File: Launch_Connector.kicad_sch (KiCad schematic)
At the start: 28 parts, among them J1 ADC1, J2 ADC2, J3 PWM, J4 GPIO

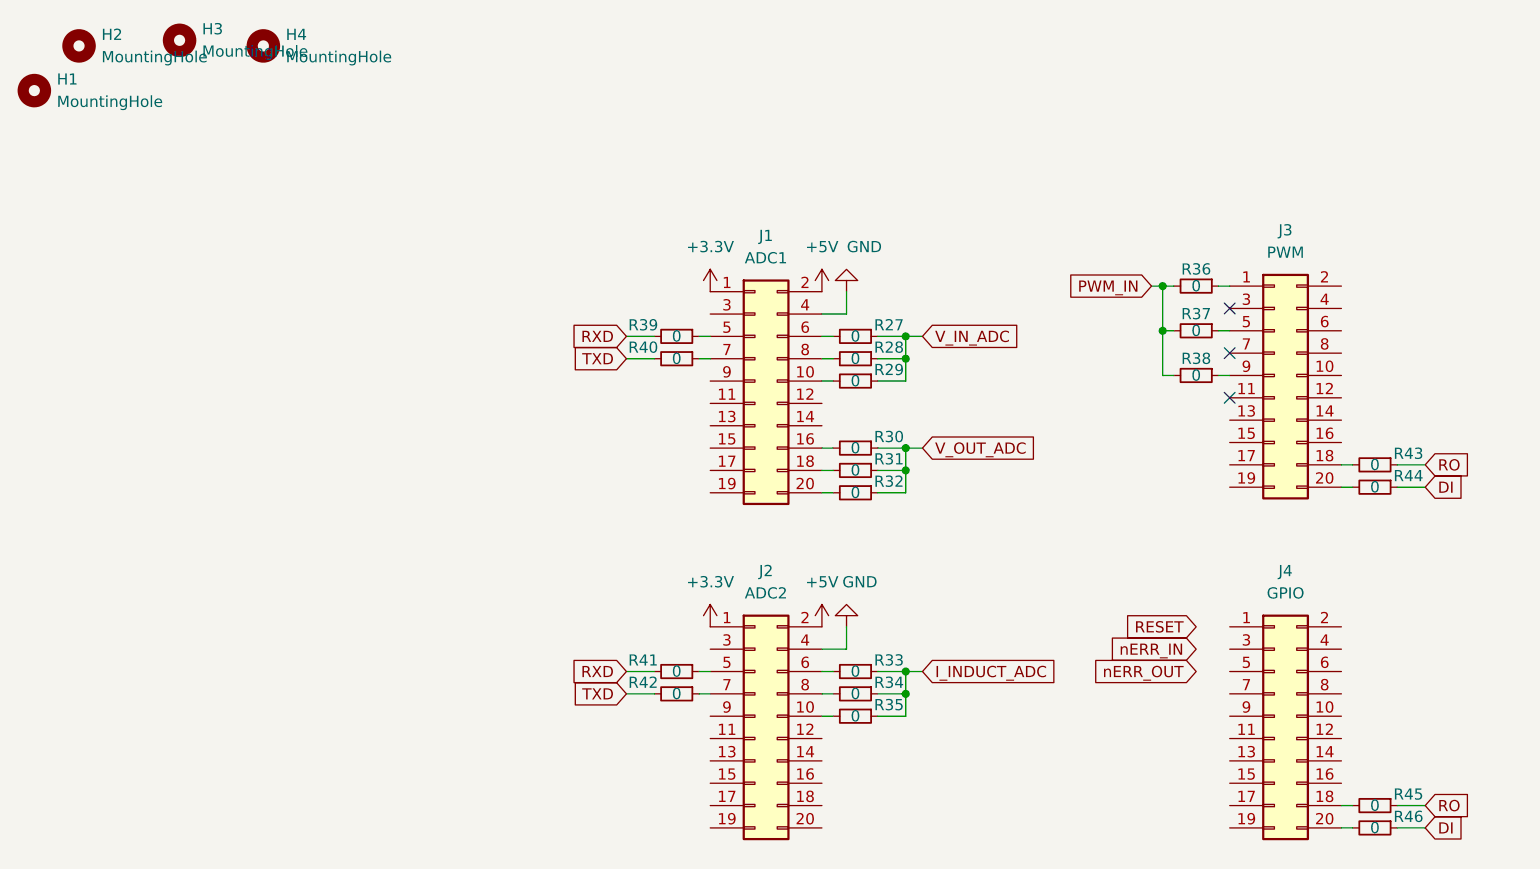
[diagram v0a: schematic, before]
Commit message: Добавил молексы и убрал питание
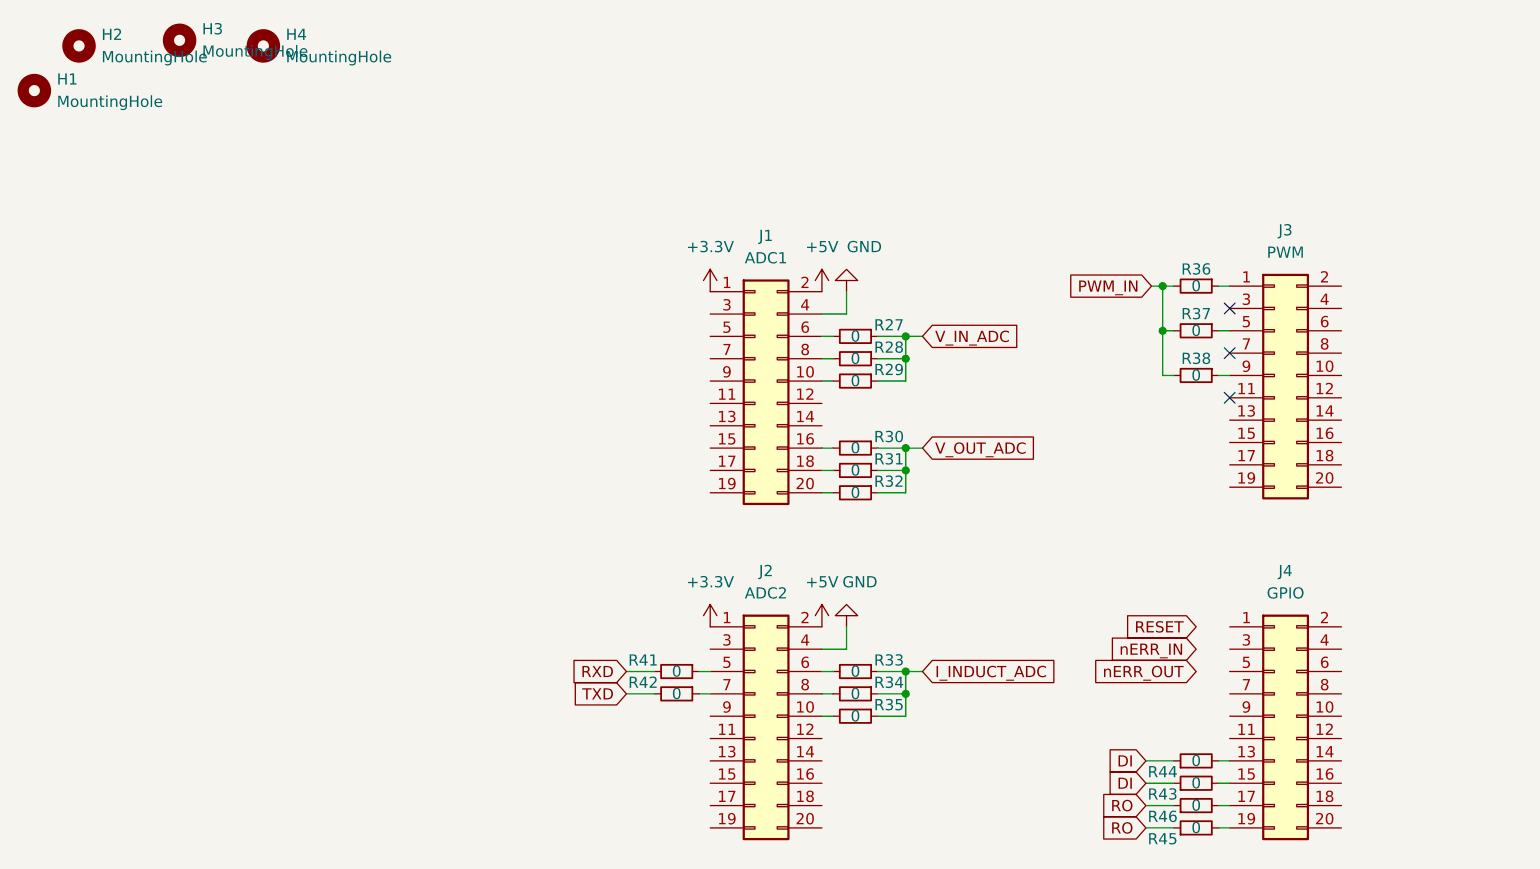
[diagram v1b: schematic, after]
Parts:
- removed R39, R40: 0, Resistor_SMD:R_0805_2012Metric_Pad1.20x1.40mm_HandSolder, symbol Device:R_Small
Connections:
- net DI: now also R43.1; no longer R46.1
- net RO: now also R46.1; no longer R43.1
- net at R45.2: now also J4.19 (Pin_19); no longer J4.18 (Pin_18)
- net at J4.13 (Pin_13): now also R44.2
- net at J4.15 (Pin_15): now also R43.2
- net at J4.17 (Pin_17): now also R46.2
- net at J4.20 (Pin_20): no longer R46.2
- net at J3.18 (Pin_18): no longer R43.2
- net at J3.20 (Pin_20): no longer R44.2
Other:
- moved on the sheet: R43, R44, R45, R46

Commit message: Первая версия в производство
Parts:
- removed R41, R42: 0, Resistor_SMD:R_0805_2012Metric_Pad1.20x1.40mm_HandSolder, symbol Device:R_Small
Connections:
- net RXD: now also J1.7 (Pin_7)
- net TXD: now also J1.5 (Pin_5)
- net at R45.2: now also J4.15 (Pin_15); no longer J4.19 (Pin_19)
- net at J4.11 (Pin_11): now also R43.2
- net at J4.13 (Pin_13): now also R46.2; no longer R44.2
- net at J4.17 (Pin_17): no longer R46.2
- net at J4.9 (Pin_9): now also R44.2
- net RESET_GPIO: now reaches J3.13 (Pin_13)
- net nERR_IN_GPIO: now reaches J3.15 (Pin_15)
- net Relay_Control: now reaches J3.18 (Pin_18)
- no-connect marks 3 -> 53
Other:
- moved on the sheet: J1, J3, R27, R28, R29, R30, R31, R32, R36, R37, R38, R43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

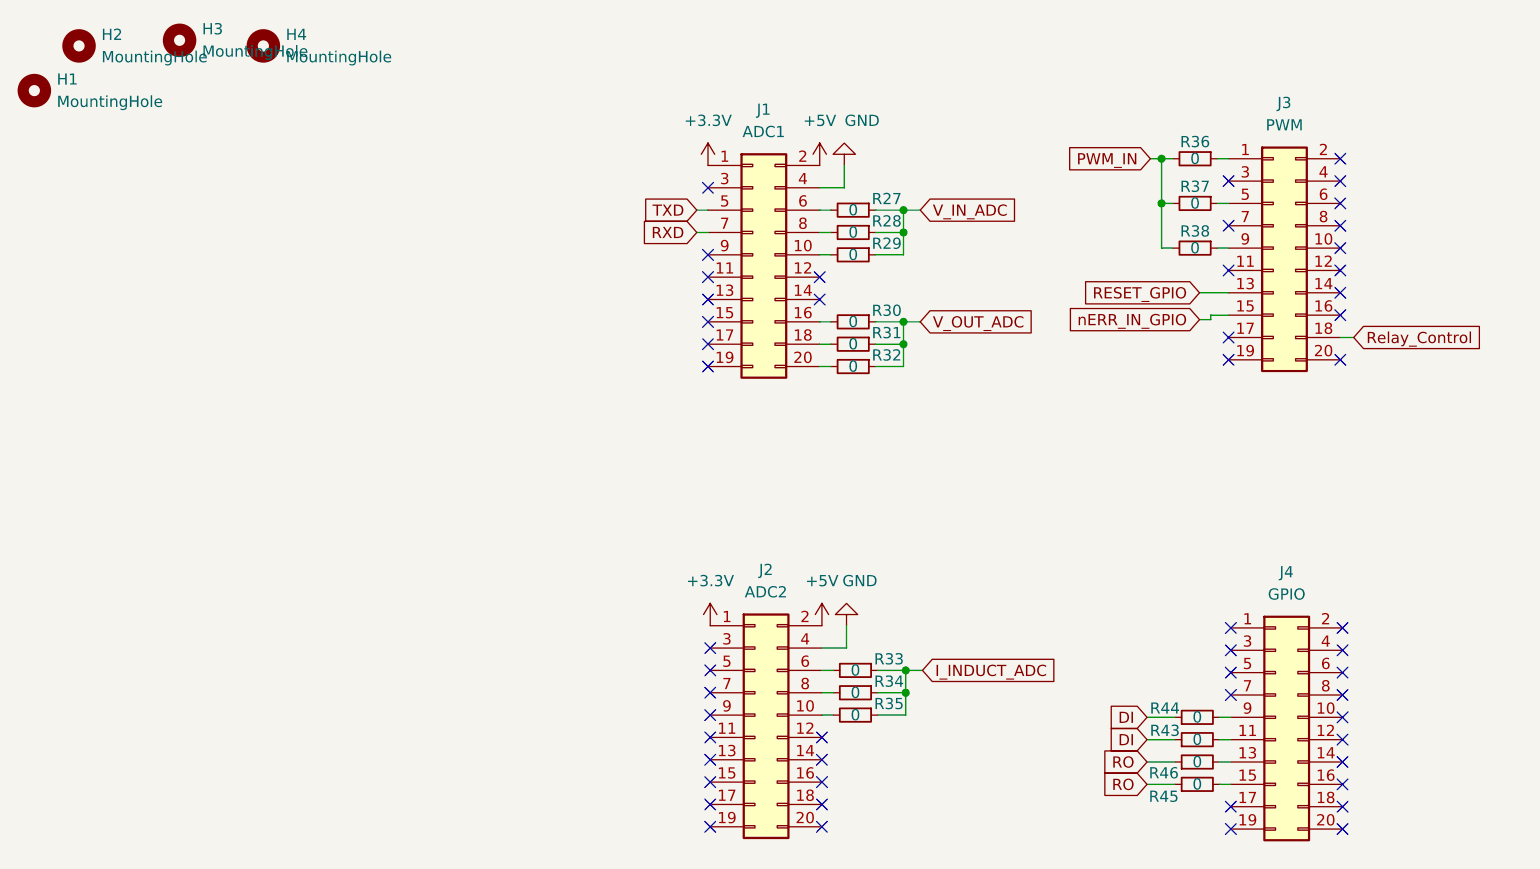
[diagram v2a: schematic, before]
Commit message: Добавил температуру, убрал подтяжки RS-485, заменил ШИМ на дифференциальный сигнал, добавил земли RS-485
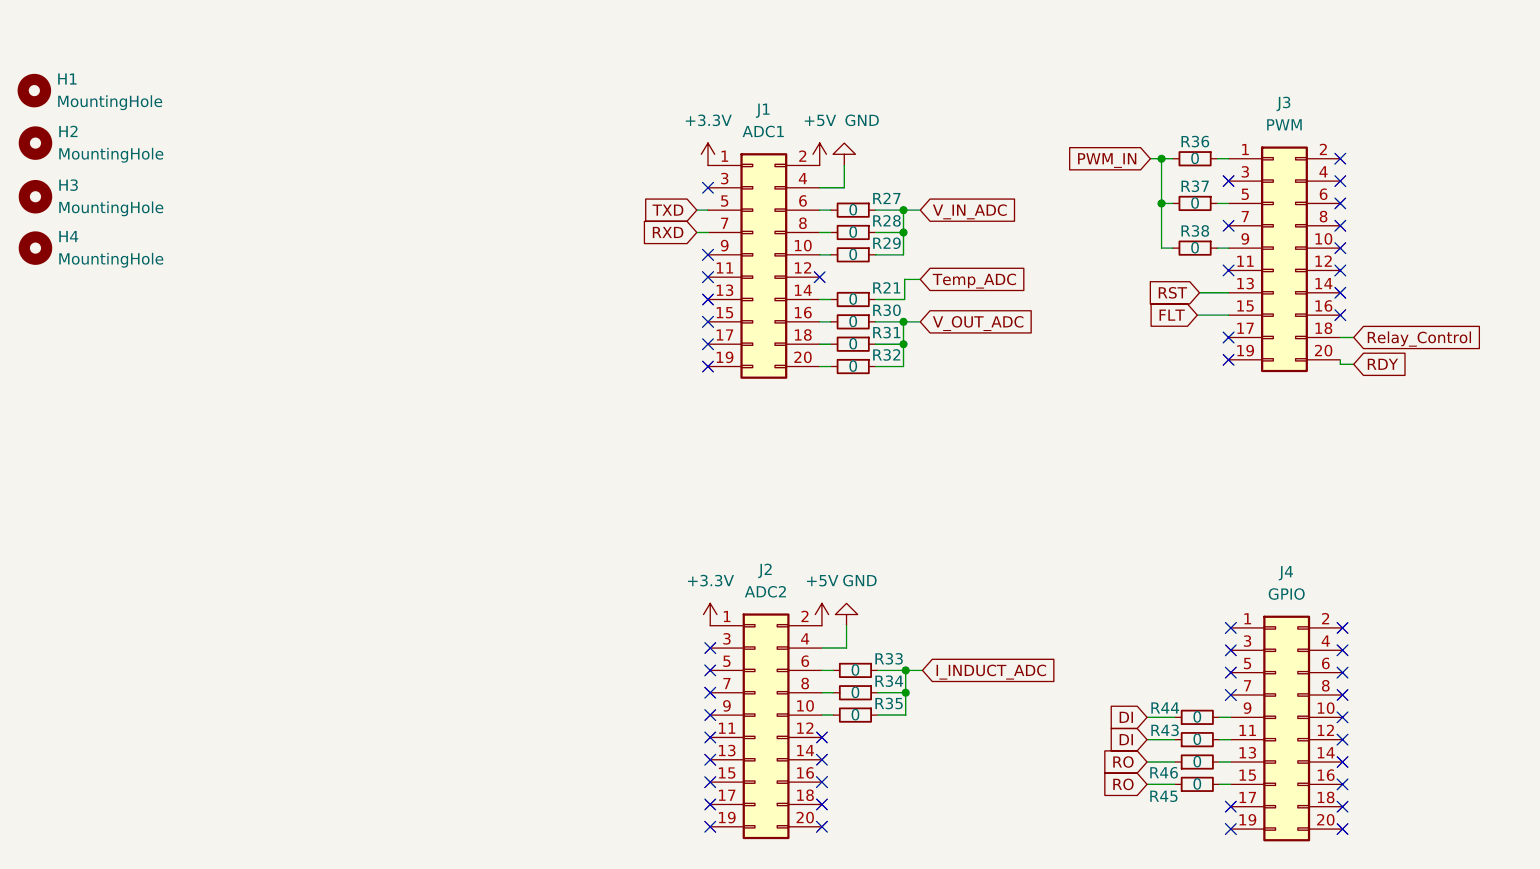
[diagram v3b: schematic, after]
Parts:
- added R21: 0, Resistor_SMD:R_0805_2012Metric_Pad1.20x1.40mm_HandSolder, symbol Device:R_Small
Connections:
- net at J1.14 (Pin_14): now also R21.2
- net RDY: now reaches J3.20 (Pin_20)
- net RESET_GPIO renamed RST
- net nERR_IN_GPIO renamed FLT
- new net Temp_ADC: R21.1
- no-connect marks 53 -> 51
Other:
- moved on the sheet: H2, H3, H4
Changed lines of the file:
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@@
   (no_connect (at 177.038 64.262))
   (no_connect (at 177.038 66.802))
-  (no_connect (at 177.038 74.422))
   (no_connect (at 177.038 69.342))
   (no_connect (at 177.038 54.102))
@@
   (no_connect (at 105.156 62.484))
   (no_connect (at 164.338 71.882))
-  (no_connect (at 117.856 67.564))
   (no_connect (at 117.856 65.024))
   (no_connect (at 164.338 54.102))
@@
     (stroke (width 0) (type default) (color 0 0 0 0))
   )
+  (wire (pts (xy 178.562 74.93) (xy 177.038 74.93))
+    (stroke (width 0) (type default) (color 0 0 0 0))
+  )
   (wire (pts (xy 118.11 107.188) (xy 120.904 107.188))
     (stroke (width 0) (type default) (color 0 0 0 0))
@@
     (stroke (width 0) (type default) (color 0 0 0 0))
   )
+  (wire (pts (xy 177.038 74.93) (xy 177.038 74.422))
+    (stroke (width 0) (type default) (color 0 0 0 0))
+  )
   (wire (pts (xy 120.65 54.864) (xy 120.65 52.324))
     (stroke (width 0) (type default) (color 0 0 0 0))
@@
     (stroke (width 0) (type default) (color 0 0 0 0))
   )
-  (wire (pts (xy 162.306 69.85) (xy 162.306 69.342))
-    (stroke (width 0) (type default) (color 0 0 0 0))
-  )
-  (wire (pts (xy 164.338 69.342) (xy 162.306 69.342))
+  (wire (pts (xy 160.782 69.342) (xy 164.338 69.342))
     (stroke (width 0) (type default) (color 0 0 0 0))
   )
@@
     (stroke (width 0) (type default) (color 0 0 0 0))
   )
-  (wire (pts (xy 161.036 69.85) (xy 162.306 69.85))
-    (stroke (width 0) (type default) (color 0 0 0 0))
-  )
   (wire (pts (xy 118.11 112.268) (xy 119.38 112.268))
     (stroke (width 0) (type default) (color 0 0 0 0))
@@
     (stroke (width 0) (type default) (color 0 0 0 0))
   )
+  (wire (pts (xy 117.856 67.564) (xy 119.126 67.564))
+    (stroke (width 0) (type default) (color 0 0 0 0))
+  )
   (wire (pts (xy 156.718 56.642) (xy 157.988 56.642))
     (stroke (width 0) (type default) (color 0 0 0 0))
@@
     (stroke (width 0) (type default) (color 0 0 0 0))
   )
+  (wire (pts (xy 127.508 65.278) (xy 127.508 67.564))
+    (stroke (width 0) (type default) (color 0 0 0 0))
+  )
   (wire (pts (xy 117.856 70.104) (xy 119.126 70.104))
     (stroke (width 0) (type default) (color 0 0 0 0))
@@
     (stroke (width 0) (type default) (color 0 0 0 0))
   )
+  (wire (pts (xy 129.286 65.278) (xy 127.508 65.278))
+    (stroke (width 0) (type default) (color 0 0 0 0))
+  )
   (wire (pts (xy 158.242 117.602) (xy 155.067 117.602))
     (stroke (width 0) (type default) (color 0 0 0 0))
@@
     (stroke (width 0) (type default) (color 0 0 0 0))
   )
+  (wire (pts (xy 127.508 67.564) (xy 124.206 67.564))
+    (stroke (width 0) (type default) (color 0 0 0 0))
+  )
   (wire (pts (xy 163.068 61.722) (xy 164.338 61.722))
     (stroke (width 0) (type default) (color 0 0 0 0))
@@
     )
   )
-  (global_label "RESET_GPIO" (shape input) (at 161.036 66.802 180) (fields_autoplaced)
-    (effects (font (size 1.27 1.27)) (justify right))
-    (property "Intersheet References" "${INTERSHEET_REFS}" (id 0) (at 147.4348 66.7226 0)
-      (effects (font (size 1.27 1.27)) (justify right) hide)
+  (global_label "RST" (shape input) (at 161.036 66.802 180) (fields_autoplaced)
+    (effects (font (size 1.27 1.27)) (justify right))
+    (property "Intersheet References" "${INTERSHEET_REFS}" (id 0) (at 155.1758 66.7226 0)
+      (effects (font (size 1.27 1.27)) (justify right) hide)
+    )
+  )
+  (global_label "RDY" (shape input) (at 178.562 74.93 0) (fields_autoplaced)
+    (effects (font (size 1.27 1.27)) (justify left))
+    (property "Intersheet References" "${INTERSHEET_REFS}" (id 0) (at 184.6037 74.8506 0)
+      (effects (font (size 1.27 1.27)) (justify left) hide)
     )
   )
@@
     )
   )
+  (global_label "Temp_ADC" (shape input) (at 129.286 65.278 0) (fields_autoplaced)
+    (effects (font (size 1.27 1.27)) (justify left))
+    (property "Intersheet References" "${INTERSHEET_REFS}" (id 0) (at 141.1939 65.1986 0)
+      (effects (font (size 1.27 1.27)) (justify left) hide)
+    )
+  )
   (global_label "PWM_IN" (shape input) (at 155.448 51.562 180) (fields_autoplaced)
     (effects (font (size 1.27 1.27)) (justify right))
@@
     )
   )
-  (global_label "nERR_IN_GPIO" (shape input) (at 161.036 69.85 180) (fields_autoplaced)
-    (effects (font (size 1.27 1.27)) (justify right))
-    (property "Intersheet References" "${INTERSHEET_REFS}" (id 0) (at 145.4391 69.7706 0)
+  (global_label "FLT" (shape input) (at 160.782 69.342 180) (fields_autoplaced)
+    (effects (font (size 1.27 1.27)) (justify right))
+    (property "Intersheet References" "${INTERSHEET_REFS}" (id 0) (at 155.2846 69.2626 0)
       (effects (font (size 1.27 1.27)) (justify right) hide)
     )
@@
     (pin "2")
   )
-  (symbol (lib_id "Mechanical:MountingHole") (at 45.085 38.1 0) (unit 1)
-    (in_bom yes) (on_board yes) (fields_autoplaced)
-    (property "Reference" "H3" (id 0) (at 47.625 36.8299 0)
+  (symbol (lib_id "Mechanical:MountingHole") (at 28.702 55.88 0) (unit 1)
+    (in_bom yes) (on_board yes) (fields_autoplaced)
+    (property "Reference" "H3" (id 0) (at 31.242 54.6099 0)
       (effects (font (size 1.27 1.27)) (justify left))
     )
-    (property "Value" "MountingHole" (id 1) (at 47.625 39.3699 0)
+    (property "Value" "MountingHole" (id 1) (at 31.242 57.1499 0)
       (effects (font (size 1.27 1.27)) (justify left))
     )
-    (property "Footprint" "MountingHole:MountingHole_3.2mm_M3" (id 2) (at 45.085 38.1 0)
-      (effects (font (size 1.27 1.27)) hide)
-    )
-    (property "Datasheet" "~" (id 3) (at 45.085 38.1 0)
+    (property "Footprint" "MountingHole:MountingHole_3.2mm_M3" (id 2) (at 28.702 55.88 0)
+      (effects (font (size 1.27 1.27)) hide)
+    )
+    (property "Datasheet" "~" (id 3) (at 28.702 55.88 0)
       (effects (font (size 1.27 1.27)) hide)
     )
@@
     (pin "9")
   )
+  (symbol (lib_id "Device:R_Small") (at 121.666 67.564 270) (unit 1)
+    (in_bom yes) (on_board yes)
+    (property "Reference" "R21" (id 0) (at 125.476 66.294 90))
+    (property "Value" "0" (id 1) (at 121.666 67.564 90))
+    (property "Footprint" "Resistor_SMD:R_0805_2012Metric_Pad1.20x1.40mm_HandSolder" (id 2) (at 121.666 67.564 0)
+      (effects (font (size 1.27 1.27)) hide)
+    )
+    (property "Datasheet" "~" (id 3) (at 121.666 67.564 0)
+      (effects (font (size 1.27 1.27)) hide)
+    )
+    (pin "1")
+    (pin "2")
+  )
   (symbol (lib_id "Device:R_Small") (at 160.528 56.642 270) (unit 1)
     (in_bom yes) (on_board yes)
@@
     (pin "1")
   )
-  (symbol (lib_id "Mechanical:MountingHole") (at 33.655 38.735 0) (unit 1)
-    (in_bom yes) (on_board yes) (fields_autoplaced)
-    (property "Reference" "H2" (id 0) (at 36.195 37.4649 0)
+  (symbol (lib_id "Mechanical:MountingHole") (at 28.702 49.784 0) (unit 1)
+    (in_bom yes) (on_board yes) (fields_autoplaced)
+    (property "Reference" "H2" (id 0) (at 31.242 48.5139 0)
       (effects (font (size 1.27 1.27)) (justify left))
     )
-    (property "Value" "MountingHole" (id 1) (at 36.195 40.0049 0)
+    (property "Value" "MountingHole" (id 1) (at 31.242 51.0539 0)
       (effects (font (size 1.27 1.27)) (justify left))
     )
-    (property "Footprint" "MountingHole:MountingHole_3.2mm_M3" (id 2) (at 33.655 38.735 0)
-      (effects (font (size 1.27 1.27)) hide)
-    )
-    (property "Datasheet" "~" (id 3) (at 33.655 38.735 0)
+    (property "Footprint" "MountingHole:MountingHole_3.2mm_M3" (id 2) (at 28.702 49.784 0)
+      (effects (font (size 1.27 1.27)) hide)
+    )
+    (property "Datasheet" "~" (id 3) (at 28.702 49.784 0)
       (effects (font (size 1.27 1.27)) hide)
     )
@@
     (pin "2")
   )
-  (symbol (lib_id "Mechanical:MountingHole") (at 54.61 38.735 0) (unit 1)
-    (in_bom yes) (on_board yes) (fields_autoplaced)
-    (property "Reference" "H4" (id 0) (at 57.15 37.4649 0)
+  (symbol (lib_id "Mechanical:MountingHole") (at 28.702 61.722 0) (unit 1)
+    (in_bom yes) (on_board yes) (fields_autoplaced)
+    (property "Reference" "H4" (id 0) (at 31.242 60.4519 0)
       (effects (font (size 1.27 1.27)) (justify left))
     )
-    (property "Value" "MountingHole" (id 1) (at 57.15 40.0049 0)
+    (property "Value" "MountingHole" (id 1) (at 31.242 62.9919 0)
       (effects (font (size 1.27 1.27)) (justify left))
     )
-    (property "Footprint" "MountingHole:MountingHole_3.2mm_M3" (id 2) (at 54.61 38.735 0)
-      (effects (font (size 1.27 1.27)) hide)
-    )
-    (property "Datasheet" "~" (id 3) (at 54.61 38.735 0)
-      (effects (font (size 1.27 1.27)) hide)
-    )
+    (property "Footprint" "MountingHole:MountingHole_3.2mm_M3" (id 2) (at 28.702 61.722 0)
+      (effects (font (size 1.27 1.27)) hide)
+    )
+    (property "Datasheet" "~" (id 3) (at 28.702 61.722 0)
+      (effects (font (size 1.27 1.27)) hide)
+    )
